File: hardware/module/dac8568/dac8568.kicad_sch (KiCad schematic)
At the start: 5 parts

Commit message: WIP module schematics: footprints, bought-part fields, and the two board projects (module-main, module-jack)
Recovered from a container restart; not yet exported or checked.

Co-Authored-By: Claude Opus 5.5 <noreply@anthropic.com>
Claude-Session: https://claude.ai/code/session_01LmB4muFXnoLprWX4JzuJ5A
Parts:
- C-DEC-DAC: footprint (none) -> Capacitor_SMD:C_0805_2012Metric; Assembly (none) -> machine; LCSC (none) -> C49678; MPN (none) -> CC0805KRX7R9BB104; Manufacturer (none) -> YAGEO
- LK-CLR: footprint (none) -> Jumper:SolderJumper-2_P1.3mm_Open_RoundedPad1.0x1.5mm; Assembly (none) -> none
- R-CLR-PU: footprint (none) -> Resistor_SMD:R_0805_2012Metric; Assembly (none) -> machine; LCSC (none) -> C17414; MPN (none) -> 0805W8F1002T5E; Manufacturer (none) -> UNI-ROYAL(Uniroyal Elec)
- R-LDAC: footprint (none) -> Resistor_SMD:R_0805_2012Metric; Assembly (none) -> machine; LCSC (none) -> C17477; MPN (none) -> 0805W8F0000T5E; Manufacturer (none) -> UNI-ROYAL(Uniroyal Elec)
- U-DAC: footprint (none) -> Package_SO:TSSOP-16_4.4x5mm_P0.65mm; Assembly (none) -> machine; LCSC (none) -> C524819; MPN (none) -> DAC8568ICPWR; Manufacturer (none) -> Texas Instruments
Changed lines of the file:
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@@
     (property "Reference" "U-DAC" (at 33.02 46.99 0) (effects (font (size 1.27 1.27))))
     (property "Value" "DAC8568ICPW" (at 48.26 46.99 0) (effects (font (size 1.27 1.27))))
-    (property "Footprint" "" (at 40.64 74.93 0) (effects (font (size 1.27 1.27)) hide))
+    (property "Footprint" "Package_SO:TSSOP-16_4.4x5mm_P0.65mm" (at 40.64 74.93 0) (effects (font (size 1.27 1.27)) hide))
     (property "Datasheet" "" (at 40.64 60.96 0) (effects (font (size 1.27 1.27)) hide))
     (property "Row" "U-DAC" (at 40.64 60.96 0) (effects (font (size 1.27 1.27)) hide))
@@
     (property "Note" "Grade C: gain-2 reference, clears to ZERO scale, and AVDD 5.0-5.5 V is a condition of the grade rather than a preference. The BOM row carries the order code, which is not the banked file's name" (at 40.64 60.96 0) (effects (font (size 1.27 1.27)) hide))
     (property "Pins_source" "datasheets/analog/DAC8568CIPW.pdf PIN DESCRIPTIONS (TSSOP-16): 1 LDAC, 2 SYNC, 3 AVDD, 4 VOUTA, 5 VOUTC, 6 VOUTE, 7 VOUTG, 8 VREFIN/VREFOUT, 9 CLR, 10 VOUTH, 11 VOUTF, 12 VOUTD, 13 VOUTB, 14 GND, 15 DIN, 16 SCLK" (at 40.64 60.96 0) (effects (font (size 1.27 1.27)) hide))
+    (property "Manufacturer" "Texas Instruments" (at 40.64 60.96 0) (effects (font (size 1.27 1.27)) hide))
+    (property "MPN" "DAC8568ICPWR" (at 40.64 60.96 0) (effects (font (size 1.27 1.27)) hide))
+    (property "LCSC" "C524819" (at 40.64 60.96 0) (effects (font (size 1.27 1.27)) hide))
+    (property "Assembly" "machine" (at 40.64 60.96 0) (effects (font (size 1.27 1.27)) hide))
     (pin "1")
     (pin "10")
@@
     (pin "8")
     (pin "9")
-    (instances (project "dac8568" (path "/b85ef4e1-b1b5-5711-b0e7-36990bb72a4d" (reference "U-DAC") (unit 1))))
+    (instances (project "module-main" (path "/fc77e9f9-9171-5c83-92ae-8cafe880764e/d3416dad-1f82-5e64-9a2d-7d16a2560a26" (reference "U3") (unit 1))) (project "dac8568" (path "/b85ef4e1-b1b5-5711-b0e7-36990bb72a4d" (reference "U-DAC") (unit 1))))
   )
   (symbol (lib_id "Device:R") (at 40.64 142.24 0) (unit 1)
@@
     (property "Reference" "R-CLR-PU" (at 43.18 140.97 0) (effects (font (size 1.27 1.27)) (justify left)))
     (property "Value" "10k 1%" (at 43.18 143.51 0) (effects (font (size 1.27 1.27)) (justify left)))
-    (property "Footprint" "" (at 39.37 142.24 0) (effects (font (size 1.27 1.27)) hide))
+    (property "Footprint" "Resistor_SMD:R_0805_2012Metric" (at 39.37 142.24 0) (effects (font (size 1.27 1.27)) hide))
     (property "Datasheet" "" (at 40.64 142.24 0) (effects (font (size 1.27 1.27)) hide))
     (property "Row" "R-CLR-PU" (at 40.64 142.24 0) (effects (font (size 1.27 1.27)) hide))
     (property "Pins" "1=1 2=2" (at 40.64 142.24 0) (effects (font (size 1.27 1.27)) hide))
     (property "Note" "PULL-UP. CLR is active low and nothing drives it, so this holds it inactive" (at 40.64 142.24 0) (effects (font (size 1.27 1.27)) hide))
+    (property "Manufacturer" "UNI-ROYAL(Uniroyal Elec)" (at 40.64 142.24 0) (effects (font (size 1.27 1.27)) hide))
+    (property "MPN" "0805W8F1002T5E" (at 40.64 142.24 0) (effects (font (size 1.27 1.27)) hide))
+    (property "LCSC" "C17414" (at 40.64 142.24 0) (effects (font (size 1.27 1.27)) hide))
+    (property "Assembly" "machine" (at 40.64 142.24 0) (effects (font (size 1.27 1.27)) hide))
     (pin "1")
     (pin "2")
-    (instances (project "dac8568" (path "/b85ef4e1-b1b5-5711-b0e7-36990bb72a4d" (reference "R-CLR-PU") (unit 1))))
+    (instances (project "module-main" (path "/fc77e9f9-9171-5c83-92ae-8cafe880764e/d3416dad-1f82-5e64-9a2d-7d16a2560a26" (reference "R8") (unit 1))) (project "dac8568" (path "/b85ef4e1-b1b5-5711-b0e7-36990bb72a4d" (reference "R-CLR-PU") (unit 1))))
   )
   (symbol (lib_id "Device:R") (at 91.44 142.24 0) (unit 1)
@@
     (property "Reference" "R-LDAC" (at 93.98 140.97 0) (effects (font (size 1.27 1.27)) (justify left)))
     (property "Value" "0R strap" (at 93.98 143.51 0) (effects (font (size 1.27 1.27)) (justify left)))
-    (property "Footprint" "" (at 90.17 142.24 0) (effects (font (size 1.27 1.27)) hide))
+    (property "Footprint" "Resistor_SMD:R_0805_2012Metric" (at 90.17 142.24 0) (effects (font (size 1.27 1.27)) hide))
     (property "Datasheet" "" (at 91.44 142.24 0) (effects (font (size 1.27 1.27)) hide))
     (property "Row" "R-LDAC" (at 91.44 142.24 0) (effects (font (size 1.27 1.27)) hide))
     (property "Pins" "1=1 2=2" (at 91.44 142.24 0) (effects (font (size 1.27 1.27)) hide))
     (property "Note" "STRAP TO GND, NOT A PULL-UP. Pin high gates the buffer-to-DAC-register transfer and no MISO exists to discover it" (at 91.44 142.24 0) (effects (font (size 1.27 1.27)) hide))
+    (property "Manufacturer" "UNI-ROYAL(Uniroyal Elec)" (at 91.44 142.24 0) (effects (font (size 1.27 1.27)) hide))
+    (property "MPN" "0805W8F0000T5E" (at 91.44 142.24 0) (effects (font (size 1.27 1.27)) hide))
+    (property "LCSC" "C17477" (at 91.44 142.24 0) (effects (font (size 1.27 1.27)) hide))
+    (property "Assembly" "machine" (at 91.44 142.24 0) (effects (font (size 1.27 1.27)) hide))
     (pin "1")
     (pin "2")
-    (instances (project "dac8568" (path "/b85ef4e1-b1b5-5711-b0e7-36990bb72a4d" (reference "R-LDAC") (unit 1))))
+    (instances (project "module-main" (path "/fc77e9f9-9171-5c83-92ae-8cafe880764e/d3416dad-1f82-5e64-9a2d-7d16a2560a26" (reference "R9") (unit 1))) (project "dac8568" (path "/b85ef4e1-b1b5-5711-b0e7-36990bb72a4d" (reference "R-LDAC") (unit 1))))
   )
   (symbol (lib_id "Device:C") (at 142.24 142.24 0) (unit 1)
@@
     (property "Reference" "C-DEC-DAC" (at 144.78 140.97 0) (effects (font (size 1.27 1.27)) (justify left)))
     (property "Value" "100nF" (at 144.78 143.51 0) (effects (font (size 1.27 1.27)) (justify left)))
-    (property "Footprint" "" (at 143.51 146.05 0) (effects (font (size 1.27 1.27)) hide))
+    (property "Footprint" "Capacitor_SMD:C_0805_2012Metric" (at 143.51 146.05 0) (effects (font (size 1.27 1.27)) hide))
     (property "Datasheet" "" (at 142.24 142.24 0) (effects (font (size 1.27 1.27)) hide))
     (property "Row" "C-DECOUPLE" (at 142.24 142.24 0) (effects (font (size 1.27 1.27)) hide))
     (property "Pins" "1=1 2=2" (at 142.24 142.24 0) (effects (font (size 1.27 1.27)) hide))
     (property "Note" "AVDD to the star, at the pin. The DAC8568 has one supply pin" (at 142.24 142.24 0) (effects (font (size 1.27 1.27)) hide))
+    (property "Manufacturer" "YAGEO" (at 142.24 142.24 0) (effects (font (size 1.27 1.27)) hide))
+    (property "MPN" "CC0805KRX7R9BB104" (at 142.24 142.24 0) (effects (font (size 1.27 1.27)) hide))
+    (property "LCSC" "C49678" (at 142.24 142.24 0) (effects (font (size 1.27 1.27)) hide))
+    (property "Assembly" "machine" (at 142.24 142.24 0) (effects (font (size 1.27 1.27)) hide))
     (pin "1")
     (pin "2")
-    (instances (project "dac8568" (path "/b85ef4e1-b1b5-5711-b0e7-36990bb72a4d" (reference "C-DEC-DAC") (unit 1))))
+    (instances (project "module-main" (path "/fc77e9f9-9171-5c83-92ae-8cafe880764e/d3416dad-1f82-5e64-9a2d-7d16a2560a26" (reference "C11") (unit 1))) (project "dac8568" (path "/b85ef4e1-b1b5-5711-b0e7-36990bb72a4d" (reference "C-DEC-DAC") (unit 1))))
   )
   (symbol (lib_id "Jumper:SolderJumper_2_Open") (at 193.04 142.24 0) (unit 1)
@@
     (property "Reference" "LK-CLR" (at 193.04 139.7 0) (effects (font (size 1.27 1.27))))
     (property "Value" "2-pad solder link" (at 193.04 144.78 0) (effects (font (size 1.27 1.27))))
-    (property "Footprint" "" (at 193.04 142.24 0) (effects (font (size 1.27 1.27)) hide))
+    (property "Footprint" "Jumper:SolderJumper-2_P1.3mm_Open_RoundedPad1.0x1.5mm" (at 193.04 142.24 0) (effects (font (size 1.27 1.27)) hide))
     (property "Datasheet" "" (at 193.04 142.24 0) (effects (font (size 1.27 1.27)) hide))
     (property "Row" "LK-CLR" (at 193.04 142.24 0) (effects (font (size 1.27 1.27)) hide))
@@
     (property "Note" "NORMALLY OPEN, and copper rather than a part. Shorted by hand it asserts CLR - the only way to assert it" (at 193.04 142.24 0) (effects (font (size 1.27 1.27)) hide))
     (property "Pins_source" "a solder link's two pads" (at 193.04 142.24 0) (effects (font (size 1.27 1.27)) hide))
+    (property "Manufacturer" "" (at 193.04 142.24 0) (effects (font (size 1.27 1.27)) hide))
+    (property "MPN" "" (at 193.04 142.24 0) (effects (font (size 1.27 1.27)) hide))
+    (property "LCSC" "" (at 193.04 142.24 0) (effects (font (size 1.27 1.27)) hide))
+    (property "Assembly" "none" (at 193.04 142.24 0) (effects (font (size 1.27 1.27)) hide))
     (pin "1")
     (pin "2")
-    (instances (project "dac8568" (path "/b85ef4e1-b1b5-5711-b0e7-36990bb72a4d" (reference "LK-CLR") (unit 1))))
+    (instances (project "module-main" (path "/fc77e9f9-9171-5c83-92ae-8cafe880764e/d3416dad-1f82-5e64-9a2d-7d16a2560a26" (reference "JP1") (unit 1))) (project "dac8568" (path "/b85ef4e1-b1b5-5711-b0e7-36990bb72a4d" (reference "LK-CLR") (unit 1))))
   )
   (wire (pts (xy 40.64 45.72) (xy 40.64 43.18)) (stroke (width 0) (type default)))

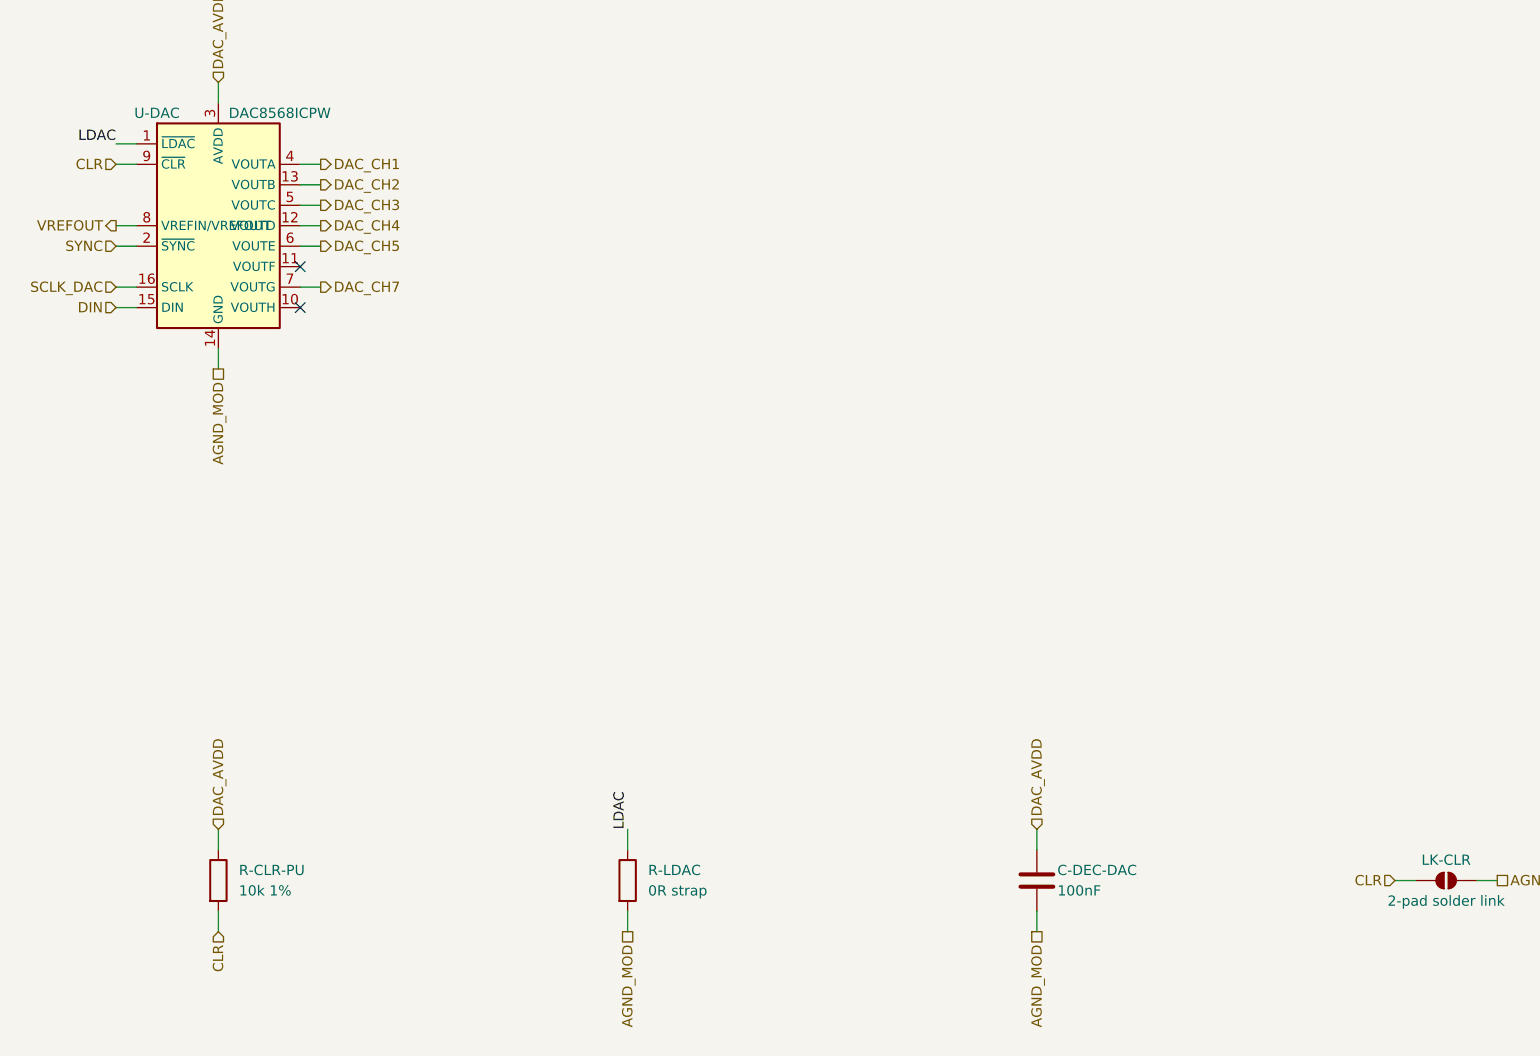
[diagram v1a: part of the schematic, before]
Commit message: dac8568: CLR is a net inside the circuit, tied inactive, not a port waiting for an unfitted part
CLR is active low and falling-edge triggered (SBAS430E p.40); R-CLR-PU ties it
to AVDD and LK-CLR asserts it by hand. The hierarchical port, the board's
no-connect sheet pin and the nets.yaml boundary entry are gone. Whether to
restore link supervision is marked as the owner's decision.

Co-Authored-By: Claude Opus 5.5 <noreply@anthropic.com>
Claude-Session: https://claude.ai/code/session_01LmB4muFXnoLprWX4JzuJ5A
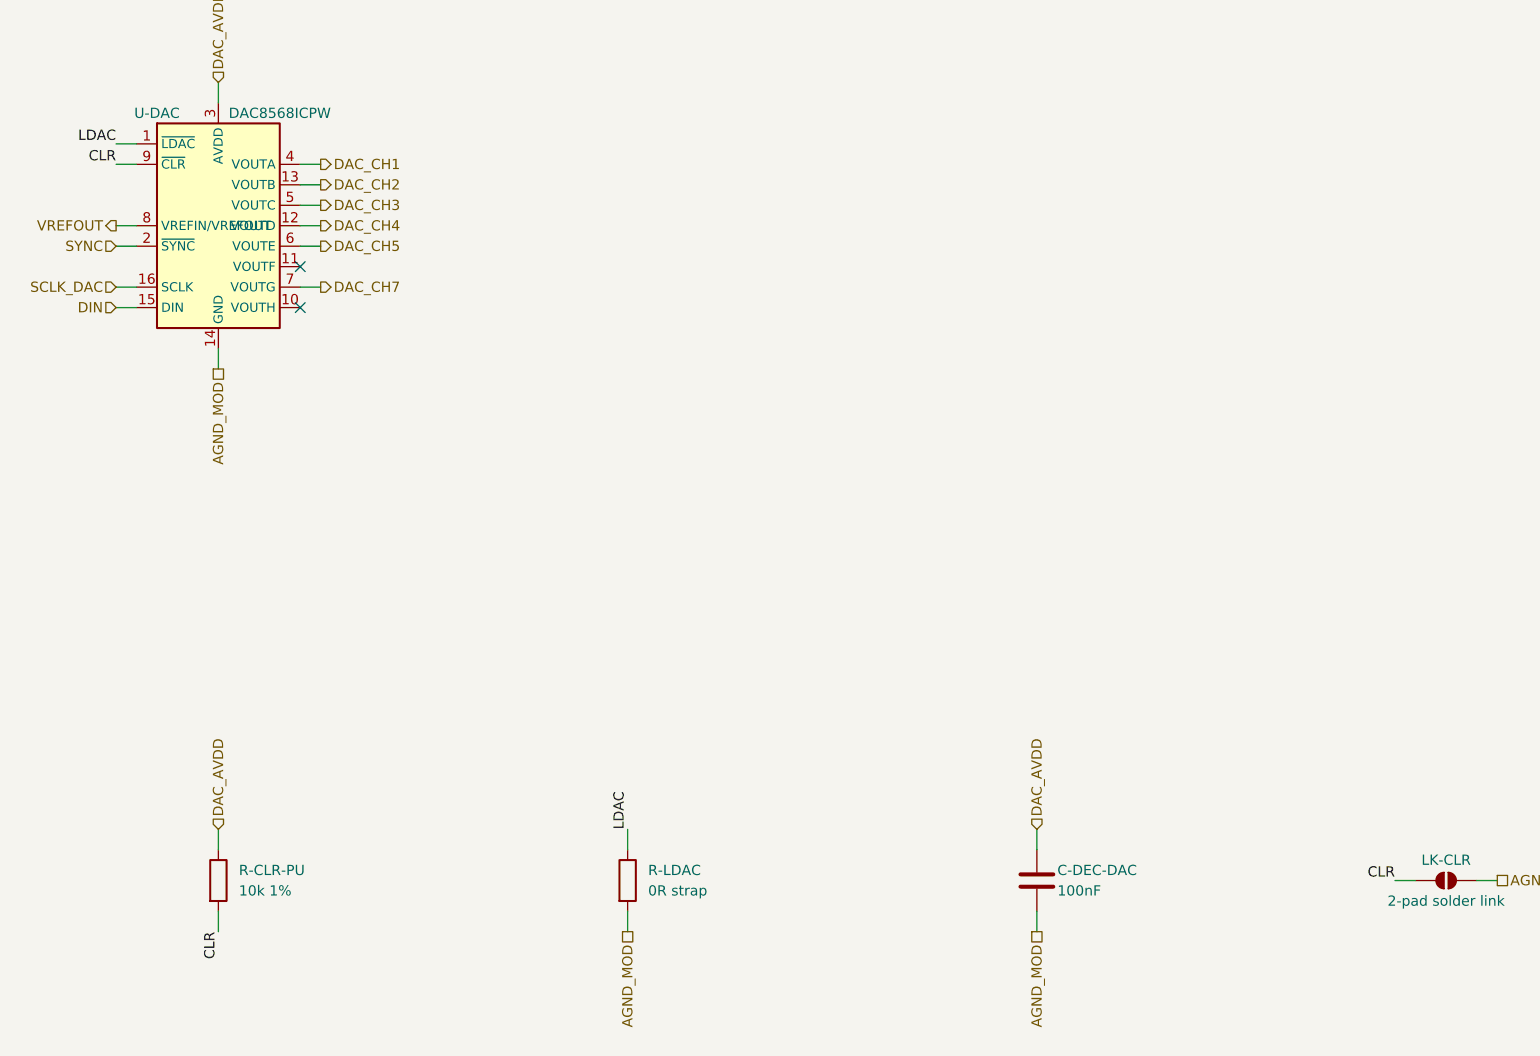
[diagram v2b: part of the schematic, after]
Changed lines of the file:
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@@
     (property "Figure" "dac-rail" (at 142.24 135.89 0) (effects (font (size 1.27 1.27)) hide)))
   (wire (pts (xy 40.64 146.05) (xy 40.64 148.59)) (stroke (width 0) (type default)))
-  (hierarchical_label "CLR" (shape input) (at 40.64 148.59 270) (effects (font (size 1.27 1.27)) (justify right))
-    (property "Dir" "in" (at 40.64 148.59 0) (effects (font (size 1.27 1.27)) hide))
-    (property "From" "module/link-supervision" (at 40.64 148.59 0) (effects (font (size 1.27 1.27)) hide)))
+  (label "CLR" (at 40.64 148.59 270) (fields_autoplaced) (effects (font (size 1.27 1.27)) (justify right bottom)))
   (wire (pts (xy 189.23 142.24) (xy 186.69 142.24)) (stroke (width 0) (type default)))
-  (hierarchical_label "CLR" (shape input) (at 186.69 142.24 180) (effects (font (size 1.27 1.27)) (justify right))
-    (property "Dir" "in" (at 186.69 142.24 0) (effects (font (size 1.27 1.27)) hide))
-    (property "From" "module/link-supervision" (at 186.69 142.24 0) (effects (font (size 1.27 1.27)) hide)))
+  (label "CLR" (at 186.69 142.24 180) (fields_autoplaced) (effects (font (size 1.27 1.27)) (justify right bottom)))
   (wire (pts (xy 30.48 53.34) (xy 27.94 53.34)) (stroke (width 0) (type default)))
-  (hierarchical_label "CLR" (shape input) (at 27.94 53.34 180) (effects (font (size 1.27 1.27)) (justify right))
-    (property "Dir" "in" (at 27.94 53.34 0) (effects (font (size 1.27 1.27)) hide))
-    (property "From" "module/link-supervision" (at 27.94 53.34 0) (effects (font (size 1.27 1.27)) hide)))
+  (label "CLR" (at 27.94 53.34 180) (fields_autoplaced) (effects (font (size 1.27 1.27)) (justify right bottom)))
   (wire (pts (xy 30.48 50.8) (xy 27.94 50.8)) (stroke (width 0) (type default)))
   (label "LDAC" (at 27.94 50.8 180) (fields_autoplaced) (effects (font (size 1.27 1.27)) (justify right bottom)))
